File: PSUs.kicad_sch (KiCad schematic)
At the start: 32 parts, among them J12 0455580003, Q1 DMP3013SFV-7, U9 AP64501SP-13

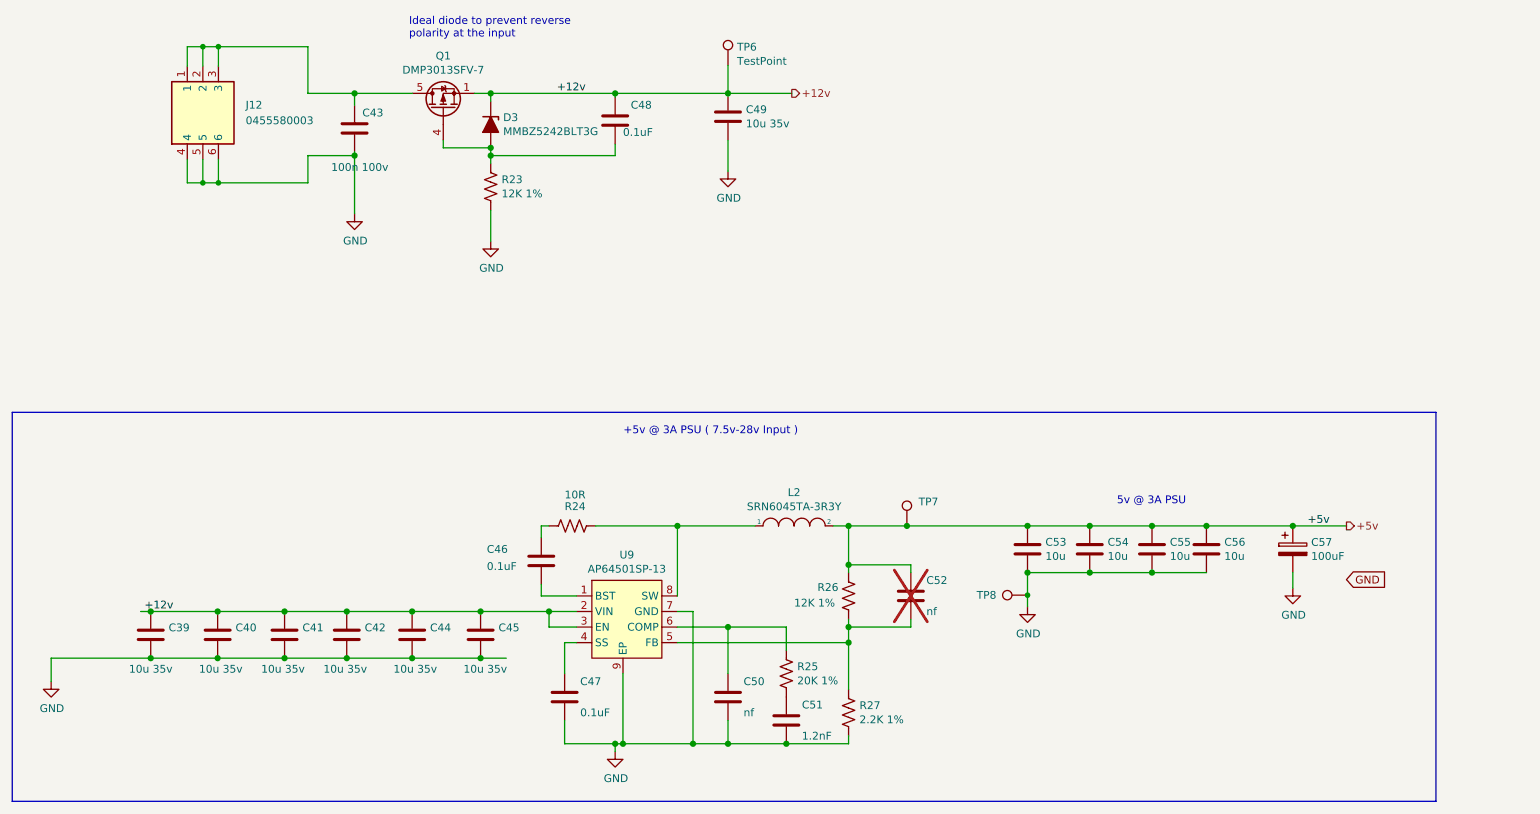
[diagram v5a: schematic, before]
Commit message: pulled in bitcrane fan and data connectors and edge cuts. most placement done. started routing
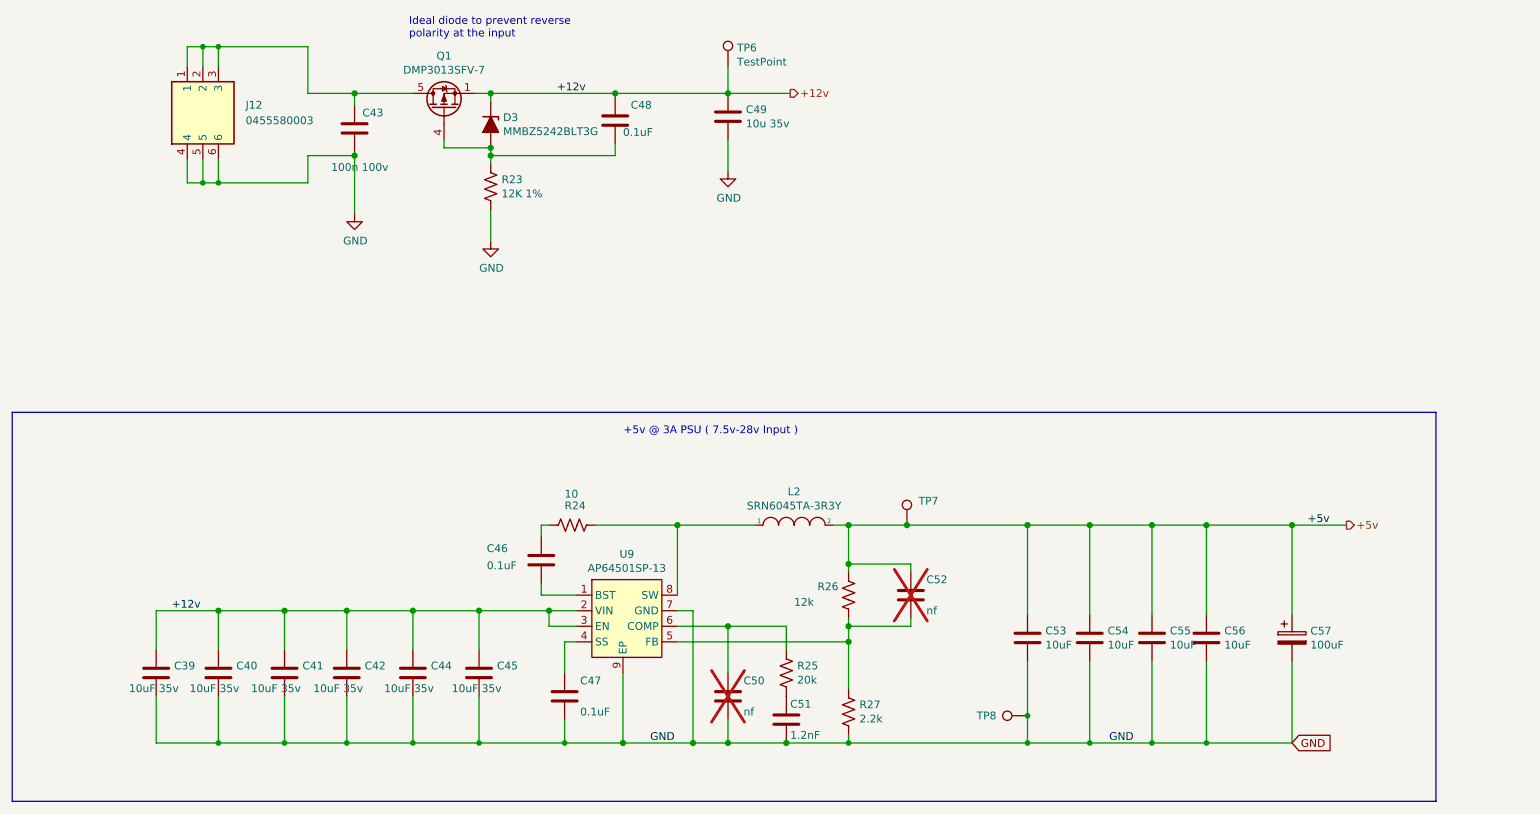
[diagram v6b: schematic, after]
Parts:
- C39, C40, C41, C42, C44, C45: value 10u 35v -> 10uF 35v
- C50: now not fitted
- C53, C54, C55, C56: value 10u -> 10uF
- R24: value 10R -> 10
- R25: value 20K 1% -> 20k
- R26: value 12K 1% -> 12k
- R27: value 2.2K 1% -> 2.2k
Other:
- note removed: "5v @ 3A PSU"
- moved on the sheet: C39, C40, C41, C42, C44, C45, C53, C54, C55, C56, C57, TP8

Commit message: lots of routing. lots more to do
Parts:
- R23: value 12K 1% -> 12k 1%
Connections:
- net +12v renamed 12V
- net +5v renamed 5V
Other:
- note added: "5V @ 3A PSU ( 7.5v-28v Input )"
- note removed: "+5v @ 3A PSU ( 7.5v-28v Input )"
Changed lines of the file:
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@@
     (effects (font (size 1.27 1.27)) (justify left bottom))
   )
-  (text "+5v @ 3A PSU ( 7.5v-28v Input )" (at 160.02 101.6 0)
+  (text "5V @ 3A PSU ( 7.5v-28v Input )" (at 160.02 101.6 0)
     (effects (font (size 1.27 1.27)) (justify right bottom))
   )
-  (label "+5v" (at 243.205 116.205 0) (fields_autoplaced)
+  (label "5V" (at 243.205 116.205 0) (fields_autoplaced)
     (effects (font (size 1.27 1.27)) (justify left bottom))
   )
@@
     (effects (font (size 1.27 1.27)) (justify left bottom))
   )
-  (label "+12v" (at 120.65 45.72 0) (fields_autoplaced)
+  (label "12V" (at 120.65 45.72 0) (fields_autoplaced)
     (effects (font (size 1.27 1.27)) (justify left bottom))
   )
@@
     (effects (font (size 1.27 1.27)) (justify left bottom))
   )
-  (label "+12v" (at 57.785 130.175 0) (fields_autoplaced)
+  (label "12V" (at 57.785 130.175 0) (fields_autoplaced)
     (effects (font (size 1.27 1.27)) (justify left bottom))
   )
@@
     )
   )
-  (hierarchical_label "+12v" (shape output) (at 158.75 45.72 0) (fields_autoplaced)
+  (hierarchical_label "12V" (shape output) (at 158.75 45.72 0) (fields_autoplaced)
     (effects (font (size 1.27 1.27)) (justify left))
   )
-  (hierarchical_label "+5v" (shape output) (at 249.555 116.205 0) (fields_autoplaced)
+  (hierarchical_label "5V" (shape output) (at 249.555 116.205 0) (fields_autoplaced)
     (effects (font (size 1.27 1.27)) (justify left))
   )
@@
       (effects (font (size 1.27 1.27)) (justify left))
     )
-    (property "Value" "12K 1%" (at 111.633 62.103 0)
-      (effects (font (size 1.27 1.27)) (justify left))
-    )
+    (property "Value" "12k 1%" (at 111.633 62.103 0)
+      (effects (font (size 1.27 1.27)) (justify left))
+    )
